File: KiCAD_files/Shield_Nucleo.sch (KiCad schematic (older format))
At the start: 2 parts, among them J1 Shield_nucleo_stage_outline, U1 NUCLEO-F401RE

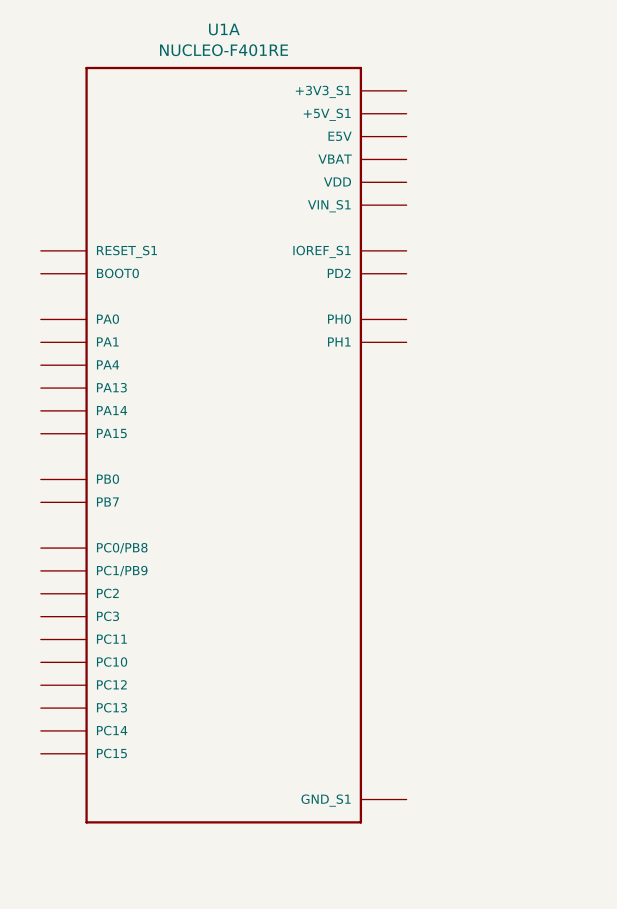
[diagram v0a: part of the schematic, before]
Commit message: Finalized BOM - Added mezzanine connectors overlay - Improved Nucleo shield
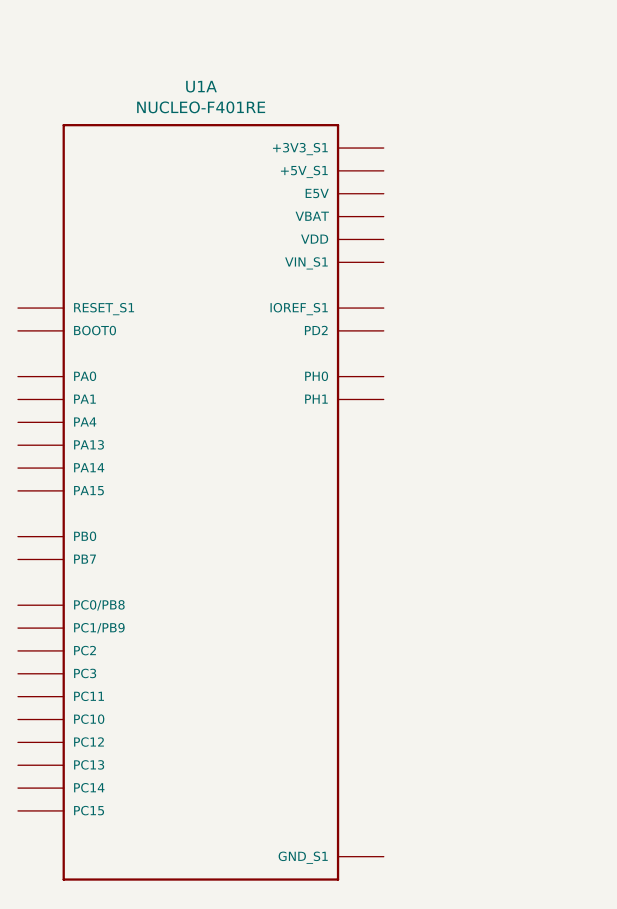
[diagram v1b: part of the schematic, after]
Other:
- moved on the sheet: U1A
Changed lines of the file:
@@
 L Symbols:NUCLEO-F401RE U1
 U 1 1 5F480C44
-P 2450 3450
-F 0 "U1" H 2450 5217 50  0000 C CNN
-F 1 "NUCLEO-F401RE" H 2450 5126 50  0000 C CNN
-F 2 "ST_NUCLEO-F401RE" H 2450 3450 50  0001 L BNN
-F 3 "Manufacturer Recommendations" H 2450 3450 50  0001 L BNN
-F 4 "13" H 2450 3450 50  0001 L BNN "Field4"
-F 5 "STMicroelectronics" H 2450 3450 50  0001 L BNN "Field5"
-F 6 "N/A" H 2450 3450 50  0001 L BNN "Field6"
-	1    2450 3450
+P 2350 3700
+F 0 "U1" H 2350 5467 50  0000 C CNN
+F 1 "NUCLEO-F401RE" H 2350 5376 50  0000 C CNN
+F 2 "ST_NUCLEO-F401RE" H 2350 3700 50  0001 L BNN
+F 3 "Manufacturer Recommendations" H 2350 3700 50  0001 L BNN
+F 4 "13" H 2350 3700 50  0001 L BNN "Field4"
+F 5 "STMicroelectronics" H 2350 3700 50  0001 L BNN "Field5"
+F 6 "N/A" H 2350 3700 50  0001 L BNN "Field6"
+	1    2350 3700
 	1    0    0    -1
 $EndComp

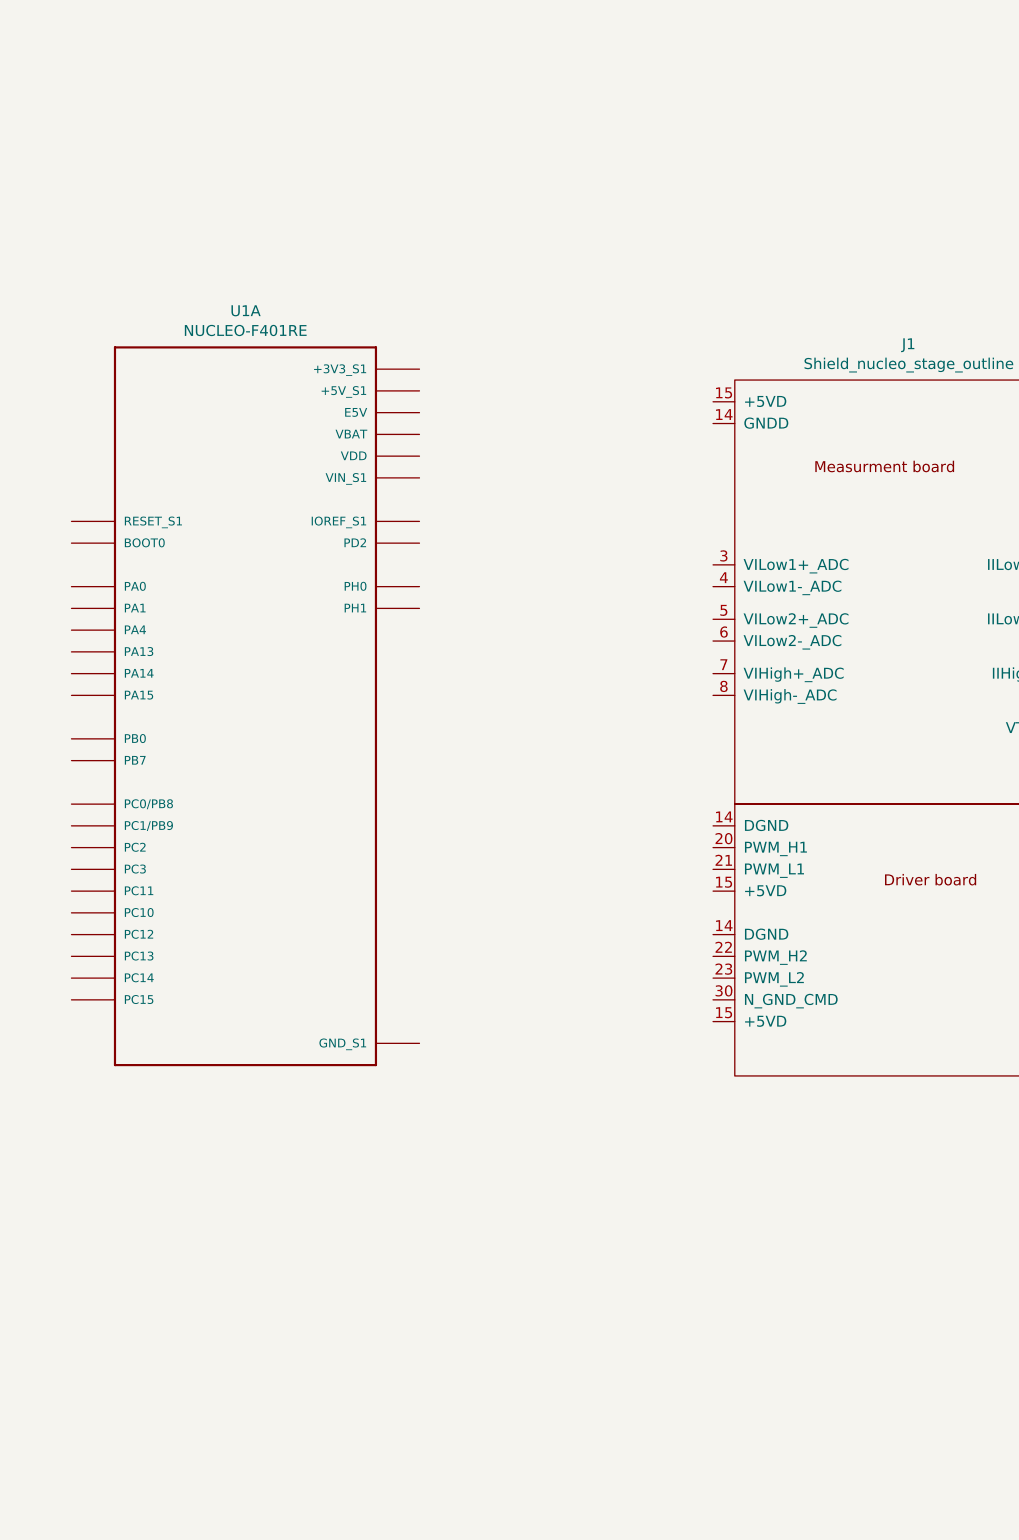
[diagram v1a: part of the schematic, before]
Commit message: Finalized overlay and added License info and current version Finalized the nucleo shield - added a CR2032 battery holder for the RTC.
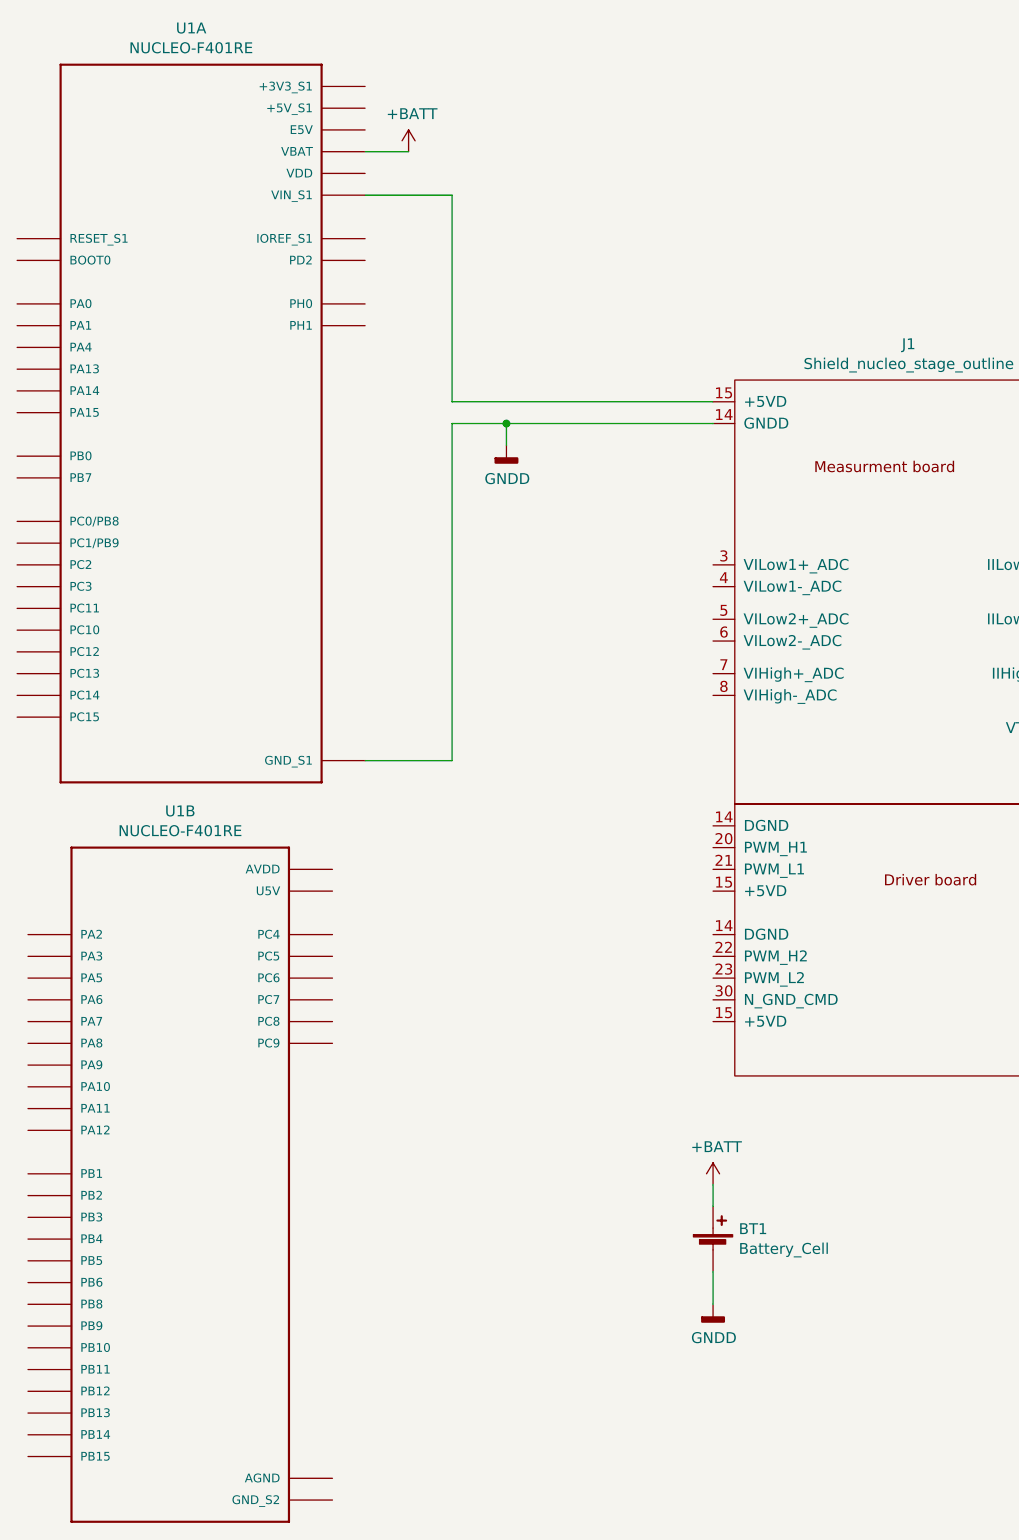
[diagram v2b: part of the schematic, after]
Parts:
- added BT1: Battery_Cell, Battery:BatteryHolder_Keystone_103_1x20mm, symbol Device:Battery_Cell
- added unit 2 of U1
- U1: footprint ST_NUCLEO-F401RE -> Footprints:ST_NUCLEO-F401RE_modified
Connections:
- net GNDD: now reaches J1.14 (GNDD)
- net GNDD: now also U1.CN7_19 (GND_S1), U1.CN7_20 (GND_S1), U1.CN7_22 (GND_S1), U1.CN7_8 (GND_S1), BT1.2 (-)
- net at J1.15 (+5VD): now also U1.CN7_24 (VIN_S1)
- net +BATT: now reaches U1.CN7_33 (VBAT)
- net +BATT: now also BT1.1 (+)
- new net: U1.CN10_20 (GND_S2), U1.CN10_9 (GND_S2)
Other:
- moved on the sheet: U1A
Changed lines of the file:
@@
 L Symbols:NUCLEO-F401RE U1
 U 1 1 5F480C44
-P 2350 3700
-F 0 "U1" H 2350 5467 50  0000 C CNN
-F 1 "NUCLEO-F401RE" H 2350 5376 50  0000 C CNN
-F 2 "ST_NUCLEO-F401RE" H 2350 3700 50  0001 L BNN
-F 3 "Manufacturer Recommendations" H 2350 3700 50  0001 L BNN
-F 4 "13" H 2350 3700 50  0001 L BNN "Field4"
-F 5 "STMicroelectronics" H 2350 3700 50  0001 L BNN "Field5"
-F 6 "N/A" H 2350 3700 50  0001 L BNN "Field6"
-	1    2350 3700
+P 2100 2400
+F 0 "U1" H 2100 4167 50  0000 C CNN
+F 1 "NUCLEO-F401RE" H 2100 4076 50  0000 C CNN
+F 2 "Footprints:ST_NUCLEO-F401RE_modified" H 2100 2400 50  0001 L BNN
+F 3 "Manufacturer Recommendations" H 2100 2400 50  0001 L BNN
+F 4 "13" H 2100 2400 50  0001 L BNN "Field4"
+F 5 "STMicroelectronics" H 2100 2400 50  0001 L BNN "Field5"
+F 6 "N/A" H 2100 2400 50  0001 L BNN "Field6"
+	1    2100 2400
 	1    0    0    -1
 $EndComp
+Wire Wire Line
+	4500 2350 3300 2350
+Wire Wire Line
+	3300 2350 3300 1400
+Wire Wire Line
+	3300 1400 2900 1400
+Wire Wire Line
+	4500 2450 3550 2450
+Wire Wire Line
+	3300 2450 3300 4000
+Wire Wire Line
+	3300 4000 2900 4000
+$Comp
+L Device:Battery_Cell BT1
+U 1 1 5F54E278
+P 4500 6250
+F 0 "BT1" H 4618 6346 50  0000 L CNN
+F 1 "Battery_Cell" H 4618 6255 50  0000 L CNN
+F 2 "Battery:BatteryHolder_Keystone_103_1x20mm" V 4500 6310 50  0001 C CNN
+F 3 "~" V 4500 6310 50  0001 C CNN
+	1    4500 6250
+	1    0    0    -1
+$EndComp
+$Comp
+L power:+BATT #PWR0101
+U 1 1 5F54F1D4
+P 4500 5950
+F 0 "#PWR0101" H 4500 5800 50  0001 C CNN
+F 1 "+BATT" H 4515 6123 50  0000 C CNN
+F 2 "" H 4500 5950 50  0001 C CNN
+F 3 "" H 4500 5950 50  0001 C CNN
+	1    4500 5950
+	1    0    0    -1
+$EndComp
+$Comp
+L power:GNDD #PWR0102
+U 1 1 5F551569
+P 4500 6500
+F 0 "#PWR0102" H 4500 6250 50  0001 C CNN
+F 1 "GNDD" H 4504 6345 50  0000 C CNN
+F 2 "" H 4500 6500 50  0001 C CNN
+F 3 "" H 4500 6500 50  0001 C CNN
+	1    4500 6500
+	1    0    0    -1
+$EndComp
+Wire Wire Line
+	4500 6350 4500 6500
+Wire Wire Line
+	4500 5950 4500 6050
+$Comp
+L power:+BATT #PWR0103
+U 1 1 5F558A3C
+P 3100 1200
+F 0 "#PWR0103" H 3100 1050 50  0001 C CNN
+F 1 "+BATT" H 3115 1373 50  0000 C CNN
+F 2 "" H 3100 1200 50  0001 C CNN
+F 3 "" H 3100 1200 50  0001 C CNN
+	1    3100 1200
+	1    0    0    -1
+$EndComp
+Wire Wire Line
+	3100 1200 2900 1200
+$Comp
+L power:GNDD #PWR0104
+U 1 1 5F55E678
+P 3550 2550
+F 0 "#PWR0104" H 3550 2300 50  0001 C CNN
+F 1 "GNDD" H 3554 2395 50  0000 C CNN
+F 2 "" H 3550 2550 50  0001 C CNN
+F 3 "" H 3550 2550 50  0001 C CNN
+	1    3550 2550
+	1    0    0    -1
+$EndComp
+Wire Wire Line
+	3550 2550 3550 2450
+Connection ~ 3550 2450
+Wire Wire Line
+	3550 2450 3300 2450
+$Comp
+L Symbols:NUCLEO-F401RE U1
+U 2 1 5F57B1FA
+P 2050 5900
+F 0 "U1" H 2050 7567 50  0000 C CNN
+F 1 "NUCLEO-F401RE" H 2050 7476 50  0000 C CNN
+F 2 "ST_NUCLEO-F401RE" H 2050 5900 50  0001 L BNN
+F 3 "Manufacturer Recommendations" H 2050 5900 50  0001 L BNN
+F 4 "13" H 2050 5900 50  0001 L BNN "Field4"
+F 5 "STMicroelectronics" H 2050 5900 50  0001 L BNN "Field5"
+F 6 "N/A" H 2050 5900 50  0001 L BNN "Field6"
+	2    2050 5900
+	1    0    0    -1
+$EndComp

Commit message: Updated shield schematic - Work in progress
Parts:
- added C? (x2): 100nF, symbol Device:C_Small
- added D? (x2): D_Schottky_Small, symbol Device:D_Schottky_Small
- added F? (x2): Polyfuse_Small, symbol Device:Polyfuse_Small
- added J? (x2): RJ45, symbol Connector:RJ45
- added JP?: Jumper, symbol Device:Jumper
- added R? (x9): R, symbol Device:R
- added TP? (x30): TestPoint, symbol Connector:TestPoint
- added U?: TCAN334, symbol Interface_CAN_LIN:TCAN334
- added U?: AT25xxx, symbol Memory_EEPROM:AT25xxx
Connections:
- net +BATT: now also TP?.1
- net GNDD: now also U1.CN10_20 (GND_S2), U1.CN10_9 (GND_S2), C?.2, C?.2, D?.1 (K), TP?.1, TP?.1, TP?.1, U?.2 (GND), U?.4 (GND)
- net at J1.10 (IILow2_ADC): now also R?.1
- net at J1.11 (IIHigh_ADC): now also R?.1
- net at J1.12 (VTh_ADC): now also R?.1
- net E5V: now reaches J1.15 (+5VD)
- net E5V: now also U1.CN7_6 (E5V)
- net at U1.CN7_24 (VIN_S1): no longer J1.15 (+5VD)
- net HRTIM1_CHA1: now reaches J1.20 (PWM_H1)
- net HRTIM1_CHA1: now also U1.CN10_23 (PA8), TP?.1
- net HRTIM1_CHA2: now reaches J1.21 (PWM_L1)
- net HRTIM1_CHA2: now also U1.CN10_21 (PA9), TP?.1
- net HRTIM1_CHB1: now reaches J1.22 (PWM_H2)
- net HRTIM1_CHB1: now also U1.CN10_33 (PA10), TP?.1
- net HRTIM1_CHB2: now reaches J1.23 (PWM_L2)
- net HRTIM1_CHB2: now also U1.CN10_14 (PA11), TP?.1
- net V1_low_P: now reaches J1.3 (VILow1+_ADC)
- net V1_low_P: now also U1.CN7_28 (PA0), TP?.1
- net V1_low_N: now reaches J1.4 (VILow1-_ADC)
- net V1_low_N: now also U1.CN7_30 (PA1), TP?.1
- net V2_low_P: now reaches J1.5 (VILow2+_ADC)
- net V2_low_P: now also U1.CN10_13 (PA6), TP?.1
- net V2_low_N: now reaches J1.6 (VILow2-_ADC)
- net V2_low_N: now also U1.CN10_15 (PA7), TP?.1
- net V_high_P: now reaches J1.7 (VIHigh+_ADC)
- net V_high_P: now also U1.CN10_6 (PC5), TP?.1
- net V_high_N: now reaches J1.8 (VIHigh-_ADC)
- net V_high_N: now also U1.CN10_22 (PB2), TP?.1
- net at J1.9 (IILow1_ADC): now also R?.1
- net SPI3_SCK: now reaches U1.CN7_1 (PC10)
- net SPI3_SCK: now also U?.6 (SCK)
- net +3V3: now reaches U1.CN7_16 (+3V3_S1)
- net +3V3: now also C?.1, C?.1, TP?.1, U?.3 (VCC), U?.8 (VCC)
- net HRTIM_EEV2: now reaches U1.CN7_2 (PC11)
- net USART1_TX: now reaches U1.CN7_21 (PB7)
- net USART1_TX: now also U1.CN10_17 (PB6)
- net HRTIM_EEV1: now reaches U1.CN7_3 (PC12)
- net EEPROM_HOLD: now reaches U1.CN7_32 (PA4)
- net EEPROM_HOLD: now also U?.7 (~HOLD)
- net I_high: now reaches U1.CN7_35 (PC2)
- net I_high: now also R?.1, R?.2, TP?.1
- net I2_low: now reaches U1.CN7_36 (PC1/PB9)
- net I2_low: now also R?.1, R?.2, TP?.1
- net EEPROM_WP: now reaches U1.CN7_37 (PC3)
- net EEPROM_WP: now also U?.3 (~WP)
- net I1_low: now reaches U1.CN7_38 (PC0/PB8)
- net I1_low: now also R?.1, R?.2, TP?.1
- net HRTIM1_CHE2: now reaches U1.CN10_1 (PC9)
- net HRTIM1_CHE2: now also TP?.1
- net HRTIM1_FLT1: now reaches U1.CN10_12 (PA12)
- net HRTIM1_CHC1: now reaches U1.CN10_16 (PB12)
- net HRTIM1_CHC1: now also TP?.1
- net N_GND: now reaches U1.CN10_18 (PB11)
- net HRTIM1_CHF2: now reaches U1.CN10_19 (PC7)
- net HRTIM1_CHF2: now also TP?.1
- net HRTIM1_CHE1: now reaches U1.CN10_2 (PC8)
- net HRTIM1_CHE1: now also TP?.1
- net CAN1_STB: now reaches U1.CN10_25 (PB10)
- net CAN1_STB: now also TP?.1, U?.8 (STB)
- net HRTIM1_CHD2: now reaches U1.CN10_26 (PB15)
- net HRTIM1_CHD2: now also TP?.1
- net SPI3_MISO: now reaches U1.CN10_27 (PB4)
- net SPI3_MISO: now also U?.2 (MISO)
- net HRTIM1_CHD1: now reaches U1.CN10_28 (PB14)
- net HRTIM1_CHD1: now also TP?.1
- net SPI3_MOSI: now reaches U1.CN10_29 (PB5)
- net SPI3_MOSI: now also U?.5 (MOSI)
- net FDCAN1_RX: now reaches U1.CN10_3 (PB8)
- net FDCAN1_RX: now also TP?.1, U?.4 (RXD)
- net HRTIM1_CHC2: now reaches U1.CN10_30 (PB13)
- net HRTIM1_CHC2: now also TP?.1
- net AGND: now reaches U1.CN10_32 (AGND)
- net AGND: now also J1.14 (GNDD), R?.2, R?.2, R?.2, R?.2
- net Temp: now reaches U1.CN10_34 (PC4)
- net Temp: now also R?.1, R?.2, TP?.1
- net HRTIM1_CHF1: now reaches U1.CN10_4 (PC6)
- net HRTIM1_CHF1: now also TP?.1
- net FDCAN1_TX: now reaches U1.CN10_5 (PB9)
- net FDCAN1_TX: now also TP?.1, U?.1 (TXD)
- new net: JP?.2, R?.1
- new net: D?.1 (K), F?.1, F?.2
- new net CAN_H: J?.1, J?.1, JP?.1, U?.7 (CANH)
- new net CAN_L: J?.2, J?.2, R?.2, U?.6 (CANL)
- new net GND_CAN: D?.2 (A), J?.3, J?.3, J?.7, J?.7
- new net PWR_CAN1: F?.2, J?.4, J?.5
- new net PWR_CAN2: F?.1, J?.4, J?.5
- new net SPI3_CS: U?.1 (~CS)
- new net V_BUS_CAN: D?.2 (A)
- no-connect marks 0 -> 5
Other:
- note added: "CAN bus power supply\n- 10V-32V\n- 600 mA (like PoE)\n\n\nDiodes necessary to prevent\nseparate GND loops.\n\nPolyfuse to prevent \nover-current in daisy-chained \nbus with multiple sources and \nsinks."
- note added: "CopyLeft LibreSolar\n"
- note added: "EEPROM - SPI\n"
- note added: "NUCLEO-G474RE Pin Mapping"
- note added: "Precision divider to adapt 5V signals to 3,3V."
- note added: "Real Time Clock \nBattery\n"
- note added: "Signal acquisition from power converter"
- moved on the sheet: BT1, J1, U1A, U1B

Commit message: Changed all the headers to improve mezzanine height
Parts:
- BT1: footprint Battery:BatteryHolder_Keystone_103_1x20mm -> TestPoint:TestPoint_Keystone_5010-5014_Multipurpose
- C1, C2: renamed from C?; footprint (none) -> Capacitor_SMD:C_0805_2012Metric
- D1, D2: renamed from D?; footprint (none) -> Diode_SMD:D_0805_2012Metric
- J2, J3: renamed from J?; footprint (none) -> Connector_RJ:RJ45_Amphenol_RJHSE538X
- JP1: renamed from JP?; footprint (none) -> Jumper:SolderJumper-2_P1.3mm_Bridged2Bar_Pad1.0x1.5mm
- R1, R2, R3, R4, R5, R6, R7, R8, R9: renamed from R?; footprint (none) -> Resistor_SMD:R_0805_2012Metric
- TP1, TP10, TP11, TP12, TP13, TP14, TP15, TP16, TP17, TP18, TP19, TP2, TP20, TP21, TP22, TP23, TP24, TP25, TP26, TP27, TP28, TP29, TP3, TP30, TP4, TP5, TP6, TP7, TP8, TP9: renamed from TP?; footprint (none) -> TestPoint:TestPoint_Plated_Hole_D2.0mm
- U1: footprint ST_NUCLEO-F401RE -> Footprints:ST_NUCLEO-F401RE_modified
- U2, U3: renamed from U?; footprint (none) -> Package_SO:SO-8_3.9x4.9mm_P1.27mm
- gave numbers to parts that had none: 2
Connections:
- net N_GND: now also J1.30 (N_GND_CMD)
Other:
- moved on the sheet: J1, R2, R3, R4, R5, R6, R7, R8, R9, TP1, TP12, TP21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
